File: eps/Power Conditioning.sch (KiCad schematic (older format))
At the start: 64 parts, among them Q10 IRF7425, Q18 IRF8302M, Q22 2N7002, Q23 2N7002, Q24 2N7002, Q25 2N7002, Q26 2N7002, Q27 2N7002, Q7 IRF7425, Q8 IRF7425, U1 ADP2303ARDZ-3.3, U2 ADP2303ARDZ-5.0, U5 LTC4365TS8, U6 LM1117-3.3, U7 MAX4373F, U8 MAX4373F, U9 MAX4373F

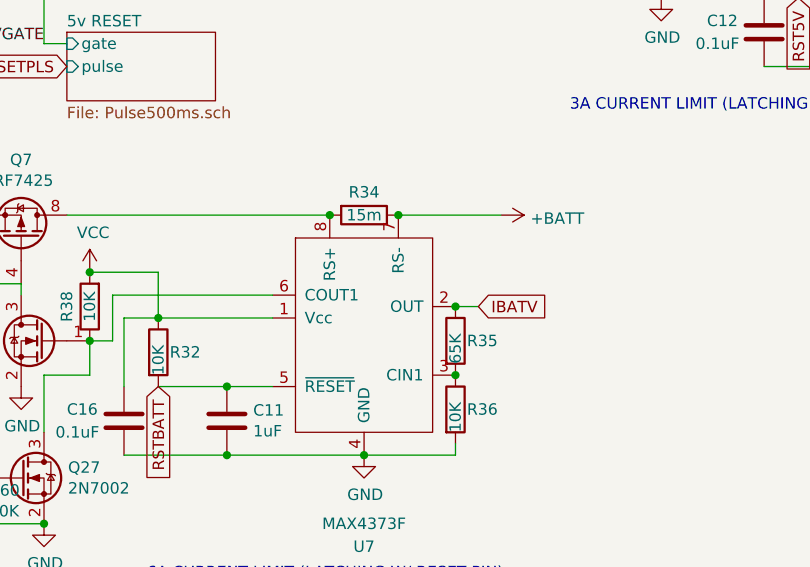
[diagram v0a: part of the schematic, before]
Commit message: start on adding LCLs to PDMs
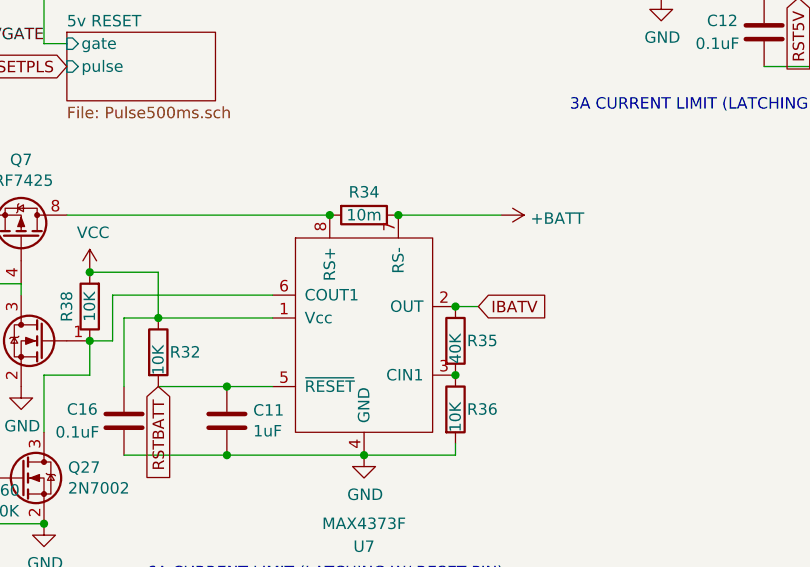
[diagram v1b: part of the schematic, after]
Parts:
- R34: value 15m -> 10m
- R35: value 65K -> 40K
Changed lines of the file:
@@
 P 6100 5350
 F 0 "R35" H 6150 5350 50  0000 L CNN
-F 1 "65K" V 6100 5250 50  0000 L CNN
+F 1 "40K" V 6100 5250 50  0000 L CNN
 F 2 "" V 6030 5350 50  0001 C CNN
 F 3 "~" H 6100 5350 50  0001 C CNN
@@
 P 5700 4800
 F 0 "R34" V 5600 4800 50  0000 C CNN
-F 1 "15m" V 5700 4800 50  0000 C CNN
+F 1 "10m" V 5700 4800 50  0000 C CNN
 F 2 "" V 5630 4800 50  0001 C CNN
 F 3 "~" H 5700 4800 50  0001 C CNN

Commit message: update pcbnew
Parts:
- C1, C10, C11, C12, C13, C14, C15, C16, C2, C3, C4, C5, C6, C7, C8, C9: footprint (none) -> Capacitor_SMD:C_0805_2012Metric_Pad1.18x1.45mm_HandSolder
- R28, R29, R30, R31, R32, R33, R34, R35, R36, R37, R38, R39, R40, R41, R42, R43, R44, R45, R46, R47, R48, R49, R50, R51, R52, R53, R60: footprint (none) -> Resistor_SMD:R_0805_2012Metric_Pad1.20x1.40mm_HandSolder
